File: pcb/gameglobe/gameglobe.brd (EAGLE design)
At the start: 98.4 x 49.5 mm, 18 parts

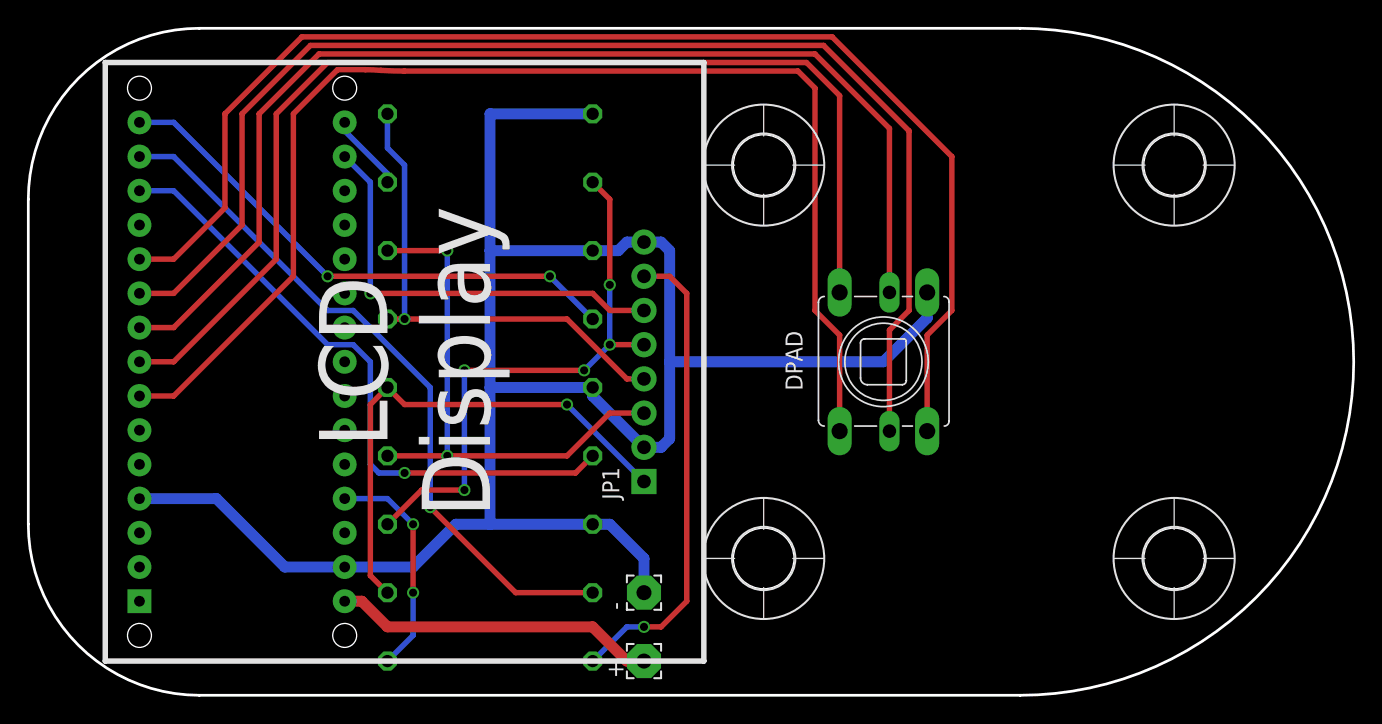
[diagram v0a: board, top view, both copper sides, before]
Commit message: Improved silkscreen
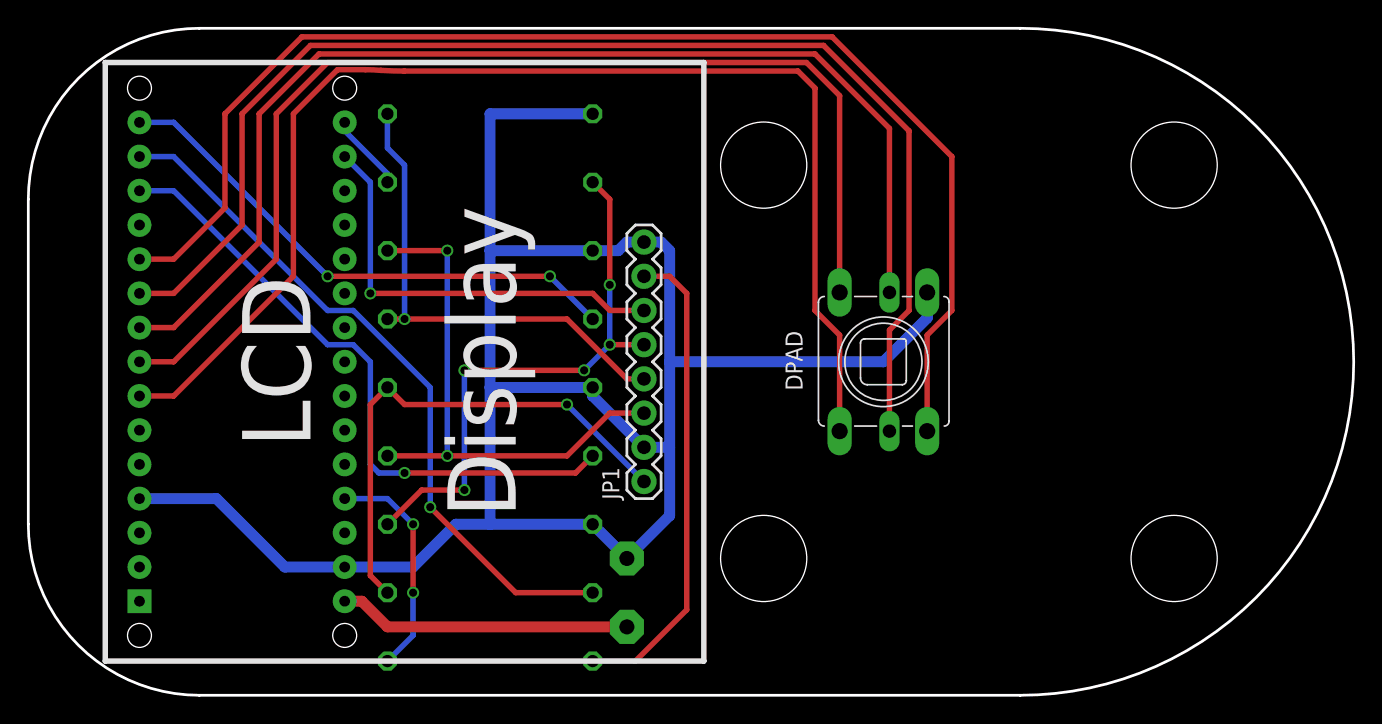
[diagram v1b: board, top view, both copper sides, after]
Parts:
- removed U$1, U$2, U$3, U$4: (no value), holes:4,5
- JP1: device SparkFun-Connectors:1X08_PIN1_NO_SILK -> SparkFun-Connectors:1X08_ROUND
- moved + 2.84 mm to (44.5, 5.71), flipped to the bottom
- moved - 2.84 mm to (44.5, 10.8), flipped to the bottom
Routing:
- net GND: track 148.6 -> 154.7 mm
- net N$7: track 24.1 -> 21.7 mm
- net LCD_LED: track 35.4 -> 35.8 mm, vias 1 -> 0
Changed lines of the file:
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@@
 <layer number="27" name="tValues" color="7" fill="1" visible="yes" active="yes"/>
 <layer number="28" name="bValues" color="7" fill="1" visible="yes" active="yes"/>
-<layer number="29" name="tStop" color="7" fill="3" visible="no" active="yes"/>
-<layer number="30" name="bStop" color="7" fill="6" visible="no" active="yes"/>
+<layer number="29" name="tStop" color="7" fill="3" visible="yes" active="yes"/>
+<layer number="30" name="bStop" color="7" fill="6" visible="yes" active="yes"/>
 <layer number="31" name="tCream" color="7" fill="4" visible="no" active="yes"/>
 <layer number="32" name="bCream" color="7" fill="5" visible="no" active="yes"/>
@@
 <wire x1="45.72" y1="13.335" x2="45.72" y2="37.465" width="0.4064" layer="22"/>
 <wire x1="45.72" y1="37.465" x2="93.98" y2="37.465" width="0.4064" layer="22"/>
-<text x="70.485" y="25.4" size="5.08" layer="26" rot="MR180" align="center">9V Battery</text>
+<text x="69.85" y="25.4" size="5.08" layer="26" font="vector" rot="MR180" align="center">9V Battery</text>
 <wire x1="0" y1="37.465" x2="12.7" y2="50.165" width="0.2032" layer="20" curve="-90"/>
 <wire x1="12.7" y1="0.635" x2="0" y2="13.335" width="0.2032" layer="20" curve="-90"/>
-<text x="15.875" y="25.4" size="4.953" layer="26" rot="SMR270" align="center">Arduino Nano</text>
+<text x="15.875" y="25.4" size="3.81" layer="26" font="vector" rot="SMR270" align="center">Arduino Nano</text>
 <wire x1="50.165" y1="47.625" x2="50.165" y2="3.175" width="0.4064" layer="21"/>
 <wire x1="50.165" y1="3.175" x2="5.715" y2="3.175" width="0.4064" layer="21"/>
 <wire x1="5.715" y1="3.175" x2="5.715" y2="47.625" width="0.4064" layer="21"/>
 <wire x1="5.715" y1="47.625" x2="50.165" y2="47.625" width="0.4064" layer="21"/>
-<text x="27.94" y="25.4" size="5.08" layer="21" rot="R90" align="center">LCD
+<text x="26.035" y="25.4" size="5.08" layer="21" font="vector" rot="R90" align="center">LCD
 Display</text>
+<hole x="54.61" y="10.795" drill="6.4"/>
+<hole x="54.61" y="40.005" drill="6.4"/>
+<hole x="85.09" y="40.005" drill="6.4"/>
+<hole x="85.09" y="10.795" drill="6.4"/>
 </plain>
 <attributes>
@@
 </autorouter>
 <elements>
-<element name="+" library="wirepad" package="2,54/1,1" value="WIREPAD2,54/1,1" x="45.72" y="3.175" rot="R90"/>
-<element name="-" library="wirepad" package="2,54/1,1" value="WIREPAD2,54/1,1" x="45.72" y="8.255" rot="R90"/>
+<element name="+" library="wirepad" package="2,54/1,1" value="WIREPAD2,54/1,1" x="44.45" y="5.715" smashed="yes" rot="MR90">
+<attribute name="NAME" x="47.244" y="5.715" size="2.54" layer="26" font="vector" ratio="10" rot="MR90" align="center"/>
+</element>
+<element name="-" library="wirepad" package="2,54/1,1" value="WIREPAD2,54/1,1" x="44.45" y="10.795" smashed="yes" rot="MR90">
+<attribute name="NAME" x="47.244" y="10.795" size="2.54" layer="26" font="vector" ratio="10" rot="MR90" align="center"/>
+</element>
 <element name="R5" library="resistor" package="0411/15" value="10k" x="34.29" y="38.735" smashed="yes" rot="MR0">
 <attribute name="VALUE" x="37.8714" y="38.1" size="1.27" layer="28" ratio="10" rot="MR0"/>
@@
 <attribute name="VALUE" x="37.8714" y="43.18" size="1.27" layer="28" ratio="10" rot="MR0"/>
 </element>
-<element name="JP1" library="SparkFun-Connectors" package="1X08_PIN1_NO_SILK" value="LCD" x="45.72" y="16.51" rot="R90"/>
+<element name="JP1" library="SparkFun-Connectors" package="1X08_ROUND" value="LCD" x="45.72" y="16.51" smashed="yes" rot="R90">
+<attribute name="NAME" x="43.8912" y="15.1638" size="1.27" layer="25" ratio="10" rot="R90"/>
+<attribute name="VALUE" x="48.895" y="15.24" size="1.27" layer="27" rot="R90"/>
+</element>
 <element name="DPAD" library="gamaral" package="SKQU" value="SKQUCAA010" x="63.5" y="25.4" smashed="yes" rot="R90">
 <attribute name="OC_MOUSER" value="688-SKQUCA" x="63.5" y="25.4" size="1.778" layer="27" rot="R90" display="off"/>
@@
 <attribute name="VALUE" x="37.8714" y="2.54" size="1.27" layer="28" ratio="10" rot="MR0"/>
 </element>
-<element name="U$1" library="holes" package="4,5" value="" x="54.61" y="10.795"/>
-<element name="U$2" library="holes" package="4,5" value="" x="54.61" y="40.005"/>
-<element name="U$3" library="holes" package="4,5" value="" x="85.09" y="10.795"/>
-<element name="U$4" library="holes" package="4,5" value="" x="85.09" y="40.005"/>
 <element name="ARDUINO_NANO" library="arduino_nano" package="PDIP-32" value="ARDUINONANO" x="8.255" y="5.08" smashed="yes" rot="MR180"/>
 </elements>
@@
 <signal name="N$7">
 <contactref element="+" pad="1"/>
-<wire x1="24.765" y1="7.62" x2="26.67" y2="5.715" width="0.8128" layer="1"/>
-<wire x1="26.67" y1="5.715" x2="41.91" y2="5.715" width="0.8128" layer="1"/>
-<wire x1="41.91" y1="5.715" x2="44.45" y2="3.175" width="0.8128" layer="1"/>
-<wire x1="44.45" y1="3.175" x2="45.72" y2="3.175" width="0.8128" layer="1"/>
 <contactref element="ARDUINO_NANO" pad="VIN"/>
+<wire x1="44.45" y1="5.715" x2="26.67" y2="5.715" width="0.8128" layer="1"/>
+<wire x1="26.67" y1="5.715" x2="24.765" y2="7.62" width="0.8128" layer="1"/>
 <wire x1="24.765" y1="7.62" x2="23.495" y2="7.62" width="0.8128" layer="1"/>
 </signal>
@@
 <contactref element="-" pad="1"/>
 <contactref element="DPAD" pad="COMMON"/>
-<wire x1="45.72" y1="8.255" x2="45.72" y2="10.795" width="0.8128" layer="16"/>
-<wire x1="45.72" y1="10.795" x2="43.18" y2="13.335" width="0.8128" layer="16"/>
-<wire x1="43.18" y1="13.335" x2="41.91" y2="13.335" width="0.8128" layer="16"/>
 <wire x1="41.91" y1="13.335" x2="34.29" y2="13.335" width="0.8128" layer="16"/>
 <wire x1="34.29" y1="13.335" x2="34.29" y2="23.495" width="0.8128" layer="16"/>
@@
 <wire x1="66.75" y1="28.65" x2="63.5" y2="25.4" width="0.8128" layer="16"/>
 <wire x1="63.5" y1="25.4" x2="47.625" y2="25.4" width="0.8128" layer="16"/>
-<wire x1="47.625" y1="25.4" x2="47.625" y2="19.685" width="0.8128" layer="16"/>
-<wire x1="47.625" y1="19.685" x2="46.99" y2="19.05" width="0.8128" layer="16"/>
-<wire x1="46.99" y1="19.05" x2="45.72" y2="19.05" width="0.8128" layer="16"/>
+<wire x1="47.625" y1="25.4" x2="47.625" y2="19.05" width="0.8128" layer="16"/>
+<wire x1="47.625" y1="19.05" x2="45.72" y2="19.05" width="0.8128" layer="16"/>
 <wire x1="45.72" y1="34.29" x2="46.99" y2="34.29" width="0.8128" layer="16"/>
 <wire x1="46.99" y1="34.29" x2="47.625" y2="33.655" width="0.8128" layer="16"/>
@@
 <wire x1="19.05" y1="10.16" x2="13.97" y2="15.24" width="0.8128" layer="16"/>
 <wire x1="13.97" y1="15.24" x2="8.255" y2="15.24" width="0.8128" layer="16"/>
+<wire x1="41.91" y1="13.335" x2="44.45" y2="10.795" width="0.8128" layer="16"/>
+<wire x1="47.625" y1="19.05" x2="47.625" y2="13.97" width="0.8128" layer="16"/>
+<wire x1="47.625" y1="13.97" x2="44.45" y2="10.795" width="0.8128" layer="16"/>
 </signal>
 <signal name="LCD_RST">
@@
 <wire x1="45.72" y1="31.75" x2="47.625" y2="31.75" width="0.4064" layer="1"/>
 <wire x1="47.625" y1="31.75" x2="48.895" y2="30.48" width="0.4064" layer="1"/>
-<wire x1="48.895" y1="30.48" x2="48.895" y2="7.62" width="0.4064" layer="1"/>
-<wire x1="48.895" y1="7.62" x2="46.99" y2="5.715" width="0.4064" layer="1"/>
-<wire x1="41.91" y1="3.175" x2="44.45" y2="5.715" width="0.4064" layer="16"/>
-<wire x1="44.45" y1="5.715" x2="45.72" y2="5.715" width="0.4064" layer="16"/>
-<via x="45.72" y="5.715" extent="1-16" drill="0.6"/>
-<wire x1="45.72" y1="5.715" x2="46.99" y2="5.715" width="0.4064" layer="1"/>
+<wire x1="48.895" y1="30.48" x2="48.895" y2="6.985" width="0.4064" layer="1"/>
+<wire x1="41.91" y1="3.175" x2="45.085" y2="3.175" width="0.4064" layer="1"/>
+<wire x1="45.085" y1="3.175" x2="48.895" y2="6.985" width="0.4064" layer="1"/>
 </signal>
 <signal name="N$1">
@@
 <wire x1="29.845" y1="23.495" x2="29.845" y2="14.605" width="0.4064" layer="16"/>
 <via x="29.845" y="14.605" extent="1-16" drill="0.6"/>
-<wire x1="37.465" y1="8.255" x2="36.195" y2="8.255" width="0" layer="19" extent="1-16"/>
 <wire x1="36.195" y1="8.255" x2="41.91" y2="8.255" width="0.4064" layer="1"/>
 <wire x1="29.845" y1="14.605" x2="36.195" y2="8.255" width="0.4064" layer="1"/>

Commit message: Added power switch to pcb. LCD pin labels on slikscreen
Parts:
- added S1: TL36YO, switch:TL3XYO
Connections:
- removed net N$7: +.1, ARDUINO_NANO.VIN
- new net N$5: ARDUINO_NANO.VIN, S1.1
- new net N$6: +.1, S1.2
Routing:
- net N$5: track 0.00 -> 34.0 mm
- net N$7: track 21.7 -> 0.00 mm
- net N$6: track 0.00 -> 13.8 mm
- net LCD_LED: track 35.8 -> 36.9 mm, vias 0 -> 1
- net LCD_DIN: track 36.7 -> 37.2 mm
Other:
- board text added: "CLK"
- board text added: "D/C"
- board text added: "DIN"
- board text added: "GND"
- board text added: "LED"
- board text added: "RST"
- board text added: "SCE"
- board text added: "VCC"
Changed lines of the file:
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@@
 <setting verticaltext="up"/>
 </settings>
-<grid distance="25" unitdist="mil" unit="mil" style="lines" multiple="1" display="yes" altdistance="0.025" altunitdist="inch" altunit="inch"/>
+<grid distance="50" unitdist="mil" unit="mil" style="lines" multiple="1" display="yes" altdistance="0.025" altunitdist="inch" altunit="inch"/>
 <layers>
 <layer number="1" name="Top" color="4" fill="1" visible="yes" active="yes"/>
@@
 <layer number="26" name="bNames" color="7" fill="1" visible="yes" active="yes"/>
 <layer number="27" name="tValues" color="7" fill="1" visible="yes" active="yes"/>
-<layer number="28" name="bValues" color="7" fill="1" visible="yes" active="yes"/>
-<layer number="29" name="tStop" color="7" fill="3" visible="yes" active="yes"/>
-<layer number="30" name="bStop" color="7" fill="6" visible="yes" active="yes"/>
+<layer number="28" name="bValues" color="7" fill="1" visible="no" active="yes"/>
+<layer number="29" name="tStop" color="7" fill="3" visible="no" active="yes"/>
+<layer number="30" name="bStop" color="7" fill="6" visible="no" active="yes"/>
 <layer number="31" name="tCream" color="7" fill="4" visible="no" active="yes"/>
 <layer number="32" name="bCream" color="7" fill="5" visible="no" active="yes"/>
@@
 <hole x="85.09" y="40.005" drill="6.4"/>
 <hole x="85.09" y="10.795" drill="6.4"/>
+<text x="47.625" y="16.51" size="0.8128" layer="25" font="vector" align="center-left">RST</text>
+<text x="47.625" y="19.05" size="0.8128" layer="25" font="vector" align="center-left">SCE</text>
+<text x="47.625" y="29.21" size="0.8128" layer="25" font="vector" align="center-left">VCC</text>
+<text x="47.625" y="24.13" size="0.8128" layer="25" font="vector" align="center-left">DIN</text>
+<text x="47.625" y="26.67" size="0.8128" layer="25" font="vector" align="center-left">CLK</text>
+<text x="47.625" y="21.59" size="0.8128" layer="25" font="vector" align="center-left">D/C</text>
+<text x="47.625" y="31.75" size="0.8128" layer="25" font="vector" align="center-left">LED</text>
+<text x="47.625" y="34.29" size="0.8128" layer="25" font="vector" align="center-left">GND</text>
 </plain>
 <attributes>
@@
 </element>
 <element name="JP1" library="SparkFun-Connectors" package="1X08_ROUND" value="LCD" x="45.72" y="16.51" smashed="yes" rot="R90">
-<attribute name="NAME" x="43.8912" y="15.1638" size="1.27" layer="25" ratio="10" rot="R90"/>
-<attribute name="VALUE" x="48.895" y="15.24" size="1.27" layer="27" rot="R90"/>
+<attribute name="VALUE" x="44.069" y="15.24" size="1.27" layer="27" font="vector" rot="R90"/>
 </element>
 <element name="DPAD" library="gamaral" package="SKQU" value="SKQUCAA010" x="63.5" y="25.4" smashed="yes" rot="R90">
@@
 </element>
 <element name="ARDUINO_NANO" library="arduino_nano" package="PDIP-32" value="ARDUINONANO" x="8.255" y="5.08" smashed="yes" rot="MR180"/>
+<element name="S1" library="switch" package="TL3XYO" value="TL36YO" x="56.515" y="3.81" smashed="yes">
+<attribute name="NAME" x="51.435" y="6.985" size="1.778" layer="25" font="vector" rot="R90" align="top-left"/>
+</element>
 </elements>
 <signals>
-<signal name="N$7">
-<contactref element="+" pad="1"/>
-<contactref element="ARDUINO_NANO" pad="VIN"/>
-<wire x1="44.45" y1="5.715" x2="26.67" y2="5.715" width="0.8128" layer="1"/>
-<wire x1="26.67" y1="5.715" x2="24.765" y2="7.62" width="0.8128" layer="1"/>
-<wire x1="24.765" y1="7.62" x2="23.495" y2="7.62" width="0.8128" layer="1"/>
-</signal>
 <signal name="GND">
 <contactref element="JP1" pad="8"/>
@@
 <wire x1="45.72" y1="24.13" x2="44.45" y2="24.13" width="0.4064" layer="1"/>
 <wire x1="44.45" y1="24.13" x2="40.005" y2="28.575" width="0.4064" layer="1"/>
-<wire x1="40.005" y1="28.575" x2="27.94" y2="28.575" width="0.4064" layer="1"/>
+<wire x1="40.005" y1="28.575" x2="29.21" y2="28.575" width="0.4064" layer="1"/>
 <wire x1="26.67" y1="43.815" x2="26.67" y2="41.275" width="0.4064" layer="16"/>
-<wire x1="26.67" y1="41.275" x2="27.94" y2="40.005" width="0.4064" layer="16"/>
-<wire x1="27.94" y1="40.005" x2="27.94" y2="28.575" width="0.4064" layer="16"/>
-<via x="27.94" y="28.575" extent="1-16" drill="0.6"/>
-<wire x1="27.94" y1="28.575" x2="26.67" y2="28.575" width="0.4064" layer="1"/>
+<wire x1="26.67" y1="41.275" x2="29.21" y2="38.735" width="0.4064" layer="16"/>
+<wire x1="29.21" y1="38.735" x2="29.21" y2="28.575" width="0.4064" layer="16"/>
+<via x="29.21" y="28.575" extent="1-16" drill="0.6"/>
+<wire x1="29.21" y1="28.575" x2="26.67" y2="28.575" width="0.4064" layer="1"/>
 </signal>
 <signal name="LCD_CLK">
@@
 <wire x1="45.72" y1="31.75" x2="47.625" y2="31.75" width="0.4064" layer="1"/>
 <wire x1="47.625" y1="31.75" x2="48.895" y2="30.48" width="0.4064" layer="1"/>
-<wire x1="48.895" y1="30.48" x2="48.895" y2="6.985" width="0.4064" layer="1"/>
-<wire x1="41.91" y1="3.175" x2="45.085" y2="3.175" width="0.4064" layer="1"/>
-<wire x1="45.085" y1="3.175" x2="48.895" y2="6.985" width="0.4064" layer="1"/>
+<wire x1="48.895" y1="30.48" x2="48.895" y2="13.97" width="0.4064" layer="1"/>
+<via x="48.895" y="13.97" extent="1-16" drill="0.6" shape="square"/>
+<wire x1="48.895" y1="13.97" x2="48.895" y2="5.08" width="0.4064" layer="16"/>
+<wire x1="48.895" y1="5.08" x2="46.99" y2="3.175" width="0.4064" layer="16"/>
+<wire x1="46.99" y1="3.175" x2="41.91" y2="3.175" width="0.4064" layer="16"/>
 </signal>
 <signal name="N$1">
@@
 <wire x1="27.9146" y1="46.99" x2="26.1874" y2="47.0408" width="0.4064" layer="1" curve="-3.369369"/>
 </signal>
+<signal name="N$5">
+<contactref element="ARDUINO_NANO" pad="VIN"/>
+<contactref element="S1" pad="1"/>
+<wire x1="53.975" y1="3.81" x2="53.975" y2="3.175" width="0.8128" layer="1"/>
+<wire x1="53.975" y1="3.175" x2="52.705" y2="1.905" width="0.8128" layer="1"/>
+<wire x1="52.705" y1="1.905" x2="30.48" y2="1.905" width="0.8128" layer="1"/>
+<wire x1="30.48" y1="1.905" x2="24.765" y2="7.62" width="0.8128" layer="1"/>
+<wire x1="24.765" y1="7.62" x2="23.495" y2="7.62" width="0.8128" layer="1"/>
+</signal>
+<signal name="N$6">
+<contactref element="S1" pad="2"/>
+<contactref element="+" pad="1"/>
+<wire x1="56.515" y1="3.81" x2="56.515" y2="4.445" width="0.8128" layer="1"/>
+<wire x1="56.515" y1="4.445" x2="54.61" y2="6.35" width="0.8128" layer="1"/>
+<wire x1="54.61" y1="6.35" x2="45.085" y2="6.35" width="0.8128" layer="1"/>
+<wire x1="45.085" y1="6.35" x2="44.45" y2="5.715" width="0.8128" layer="1"/>
+</signal>
 </signals>

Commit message: Set LED resistor value to 100 (after testing with prototype); Move some silkscreen items around; Enable all needed layers in Eagle
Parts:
- R1: value 220 -> 100
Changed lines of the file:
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@@
 <layer number="26" name="bNames" color="7" fill="1" visible="yes" active="yes"/>
 <layer number="27" name="tValues" color="7" fill="1" visible="yes" active="yes"/>
-<layer number="28" name="bValues" color="7" fill="1" visible="no" active="yes"/>
+<layer number="28" name="bValues" color="7" fill="1" visible="yes" active="yes"/>
 <layer number="29" name="tStop" color="7" fill="3" visible="no" active="yes"/>
 <layer number="30" name="bStop" color="7" fill="6" visible="no" active="yes"/>
@@
 <layer number="43" name="vRestrict" color="2" fill="10" visible="no" active="yes"/>
 <layer number="44" name="Drills" color="7" fill="1" visible="no" active="yes"/>
-<layer number="45" name="Holes" color="7" fill="1" visible="no" active="yes"/>
+<layer number="45" name="Holes" color="7" fill="1" visible="yes" active="yes"/>
 <layer number="46" name="Milling" color="3" fill="1" visible="no" active="yes"/>
 <layer number="47" name="Measures" color="7" fill="1" visible="no" active="yes"/>
@@
 <text x="26.035" y="25.4" size="5.08" layer="21" font="vector" rot="R90" align="center">LCD
 Display</text>
-<hole x="54.61" y="10.795" drill="6.4"/>
-<hole x="54.61" y="40.005" drill="6.4"/>
-<hole x="85.09" y="40.005" drill="6.4"/>
-<hole x="85.09" y="10.795" drill="6.4"/>
 <text x="47.625" y="16.51" size="0.8128" layer="25" font="vector" align="center-left">RST</text>
 <text x="47.625" y="19.05" size="0.8128" layer="25" font="vector" align="center-left">SCE</text>
@@
 <text x="47.625" y="31.75" size="0.8128" layer="25" font="vector" align="center-left">LED</text>
 <text x="47.625" y="34.29" size="0.8128" layer="25" font="vector" align="center-left">GND</text>
+<hole x="54.61" y="40.64" drill="5.08"/>
+<hole x="54.61" y="10.16" drill="5.08"/>
+<hole x="85.09" y="10.16" drill="5.08"/>
+<hole x="85.09" y="40.64" drill="5.08"/>
 </plain>
 <attributes>
@@
 <attribute name="NAME" x="57.5" y="25.48" size="1.27" layer="25" rot="R90" align="bottom-center"/>
 </element>
-<element name="R1" library="resistor" package="0411/15" value="220" x="34.29" y="3.175" smashed="yes" rot="MR0">
+<element name="R1" library="resistor" package="0411/15" value="100" x="34.29" y="3.175" smashed="yes" rot="MR0">
 <attribute name="VALUE" x="37.8714" y="2.54" size="1.27" layer="28" ratio="10" rot="MR0"/>
 </element>
 <element name="ARDUINO_NANO" library="arduino_nano" package="PDIP-32" value="ARDUINONANO" x="8.255" y="5.08" smashed="yes" rot="MR180"/>
 <element name="S1" library="switch" package="TL3XYO" value="TL36YO" x="56.515" y="3.81" smashed="yes">
-<attribute name="NAME" x="51.435" y="6.985" size="1.778" layer="25" font="vector" rot="R90" align="top-left"/>
+<attribute name="NAME" x="61.595" y="6.985" size="1.778" layer="25" font="vector" rot="R90"/>
 </element>
 </elements>
